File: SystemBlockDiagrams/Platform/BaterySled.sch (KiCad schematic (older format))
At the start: 7 parts

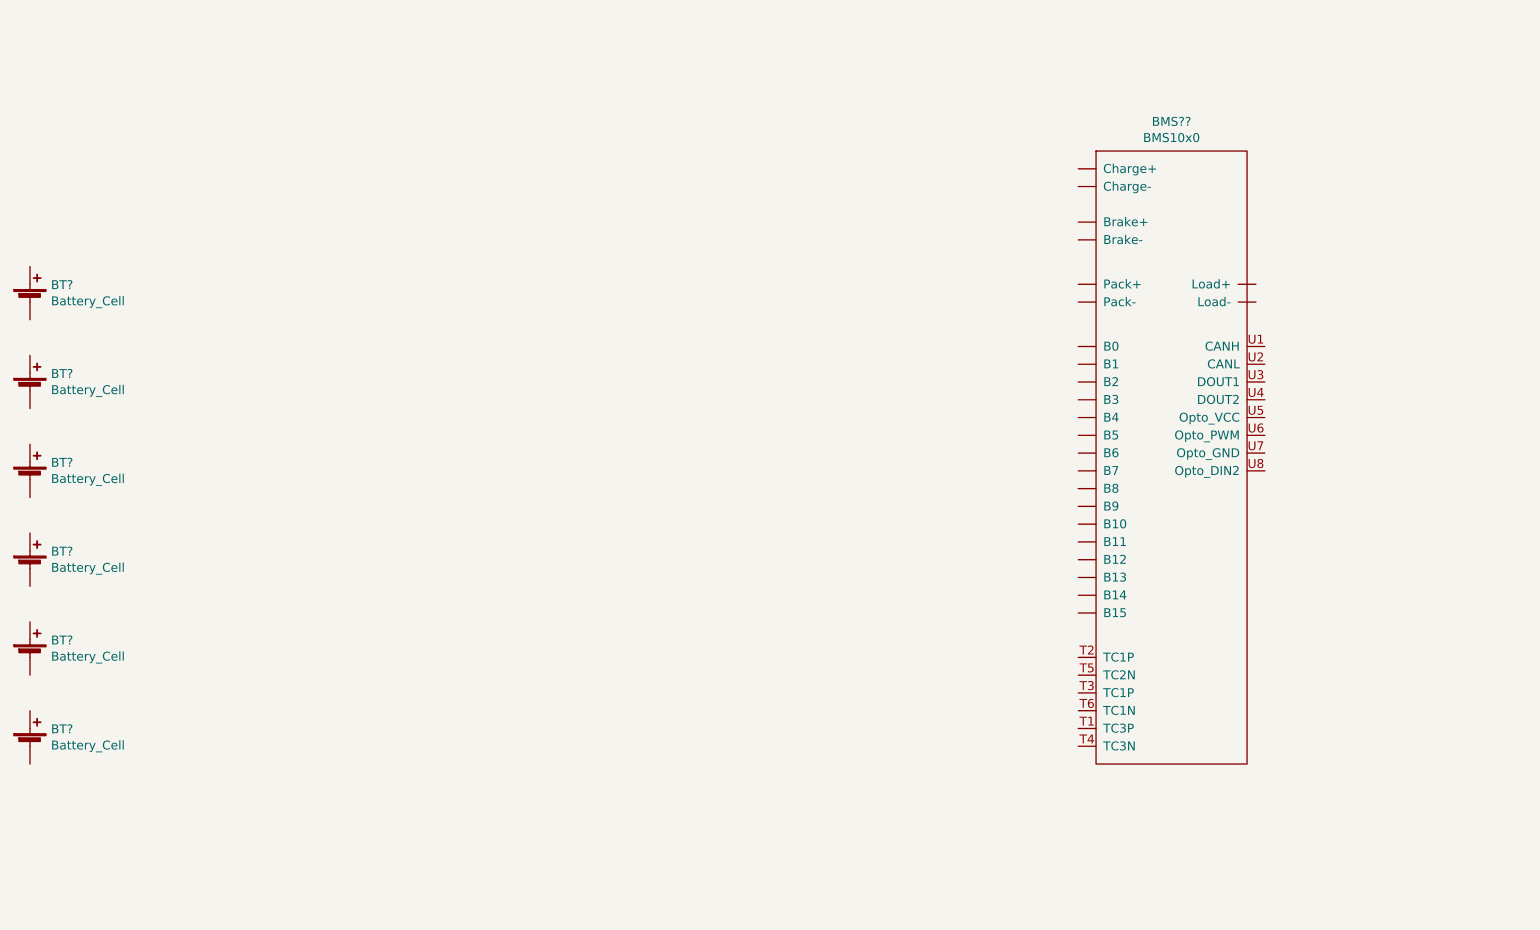
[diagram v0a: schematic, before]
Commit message: More platorm parts and connectors
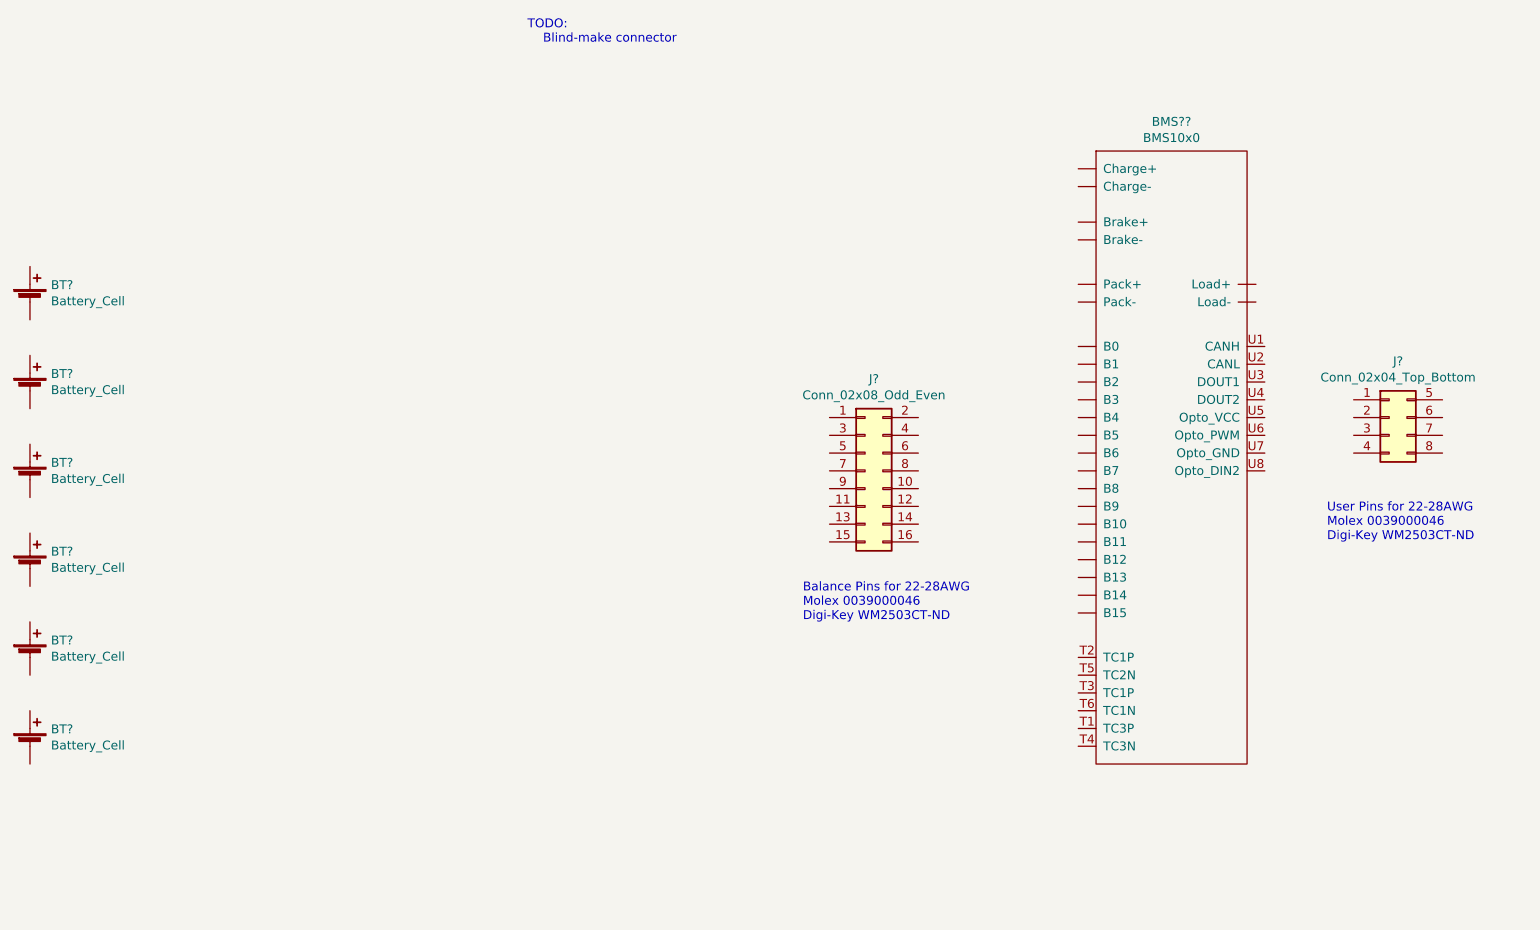
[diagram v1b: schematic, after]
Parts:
- added J?: Conn_02x08_Odd_Even, symbol Connector_Generic:Conn_02x08_Odd_Even
- added J?: Conn_02x04_Top_Bottom, symbol Connector_Generic:Conn_02x04_Top_Bottom
- BMS??: Supplier (none) -> Roboteq; Supplier Part Number (none) -> BMS1040
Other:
- note added: "Balance Pins for 22-28AWG\nMolex 0039000046\nDigi-Key WM2503CT-ND"
- note added: "TODO:\n Blind-make connector"
- note added: "User Pins for 22-28AWG\nMolex 0039000046\nDigi-Key WM2503CT-ND"
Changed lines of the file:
@@
 F 1 "BMS10x0" H 8175 3074 50  0000 C CNN
 F 2 "" H 7950 2350 50  0001 C CNN
-F 3 "" H 7950 2350 50  0001 C CNN
+F 3 "https://www.roboteq.com/index.php/docman/bms-documents-and-files/bms-documents/datasheet/349-bms10x0-datasheet/file" H 7950 2350 50  0001 C CNN
+F 4 "Roboteq" H 7950 2350 50  0001 C CNN "Supplier"
+F 5 "BMS1040" H 7950 2350 50  0001 C CNN "Supplier Part Number"
 	1    7950 2350
 	1    0    0    -1
@@
 	1    0    0    -1
 $EndComp
+Text Notes 4550 1100 0    50   ~ 0
+TODO:\n    Blind-make connector
+$Comp
+L Connector_Generic:Conn_02x08_Odd_Even J?
+U 1 1 5E27E551
+P 6450 3500
+F 0 "J?" H 6500 4017 50  0000 C CNN
+F 1 "Conn_02x08_Odd_Even" H 6500 3926 50  0000 C CNN
+F 2 "" H 6450 3500 50  0001 C CNN
+F 3 "https://www.molex.com/pdm_docs/sd/039012160_sd.pdf" H 6450 3500 50  0001 C CNN
+F 4 "Molex" H 6450 3500 50  0001 C CNN "Manufacturer"
+F 5 "0039012160" H 6450 3500 50  0001 C CNN "Manufacturer Part Number"
+F 6 "Digi-Key" H 6450 3500 50  0001 C CNN "Supplier"
+F 7 "WM3707-ND" H 6450 3500 50  0001 C CNN "Supplier Part Number"
+	1    6450 3500
+	1    0    0    -1
+$EndComp
+Text Notes 6100 4350 0    50   ~ 0
+Balance Pins for 22-28AWG\nMolex 0039000046\nDigi-Key WM2503CT-ND
+$Comp
+L Connector_Generic:Conn_02x04_Top_Bottom J?
+U 1 1 5E28024A
+P 9400 3200
+F 0 "J?" H 9450 3517 50  0000 C CNN
+F 1 "Conn_02x04_Top_Bottom" H 9450 3426 50  0000 C CNN
+F 2 "" H 9400 3200 50  0001 C CNN
+F 3 "https://www.molex.com/pdm_docs/sd/039012080_sd.pdf" H 9400 3200 50  0001 C CNN
+F 4 "Molex" H 9400 3200 50  0001 C CNN "Manufacturer"
+F 5 "0039012080" H 9400 3200 50  0001 C CNN "Manufacturer Part Number"
+F 6 "Digi-Key" H 9400 3200 50  0001 C CNN "Supplier"
+F 7 "WM3703-ND" H 9400 3200 50  0001 C CNN "Supplier Part Number"
+	1    9400 3200
+	1    0    0    -1
+$EndComp
+Text Notes 9050 3900 0    50   ~ 0
+User Pins for 22-28AWG\nMolex 0039000046\nDigi-Key WM2503CT-ND
 $EndSCHEMATC

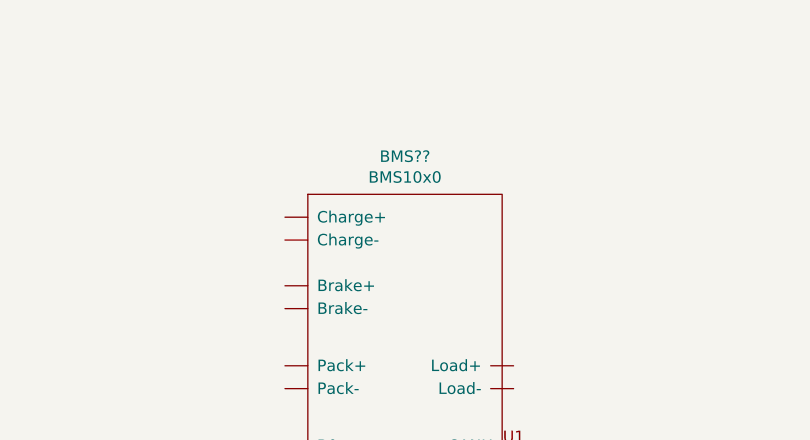
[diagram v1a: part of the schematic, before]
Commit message: Adjust electronics hierarchy to match mechanicals.
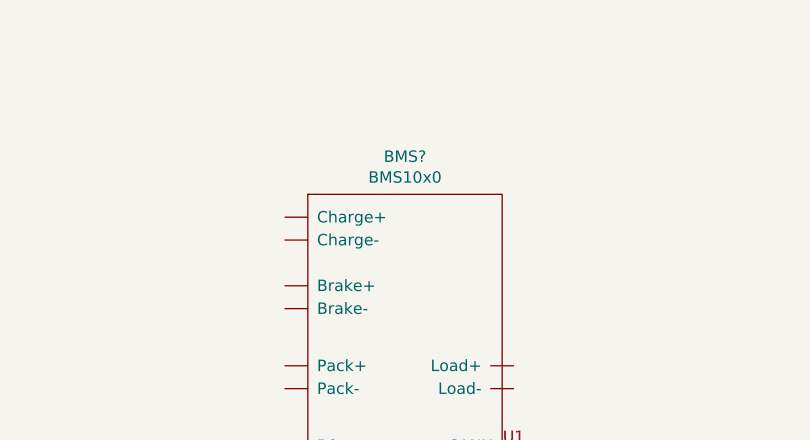
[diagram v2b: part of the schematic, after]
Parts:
- gave numbers to parts that had none: 1
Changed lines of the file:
@@
 $Descr A4 11693 8268
 encoding utf-8
-Sheet 15 15
+Sheet 15 16
 Title ""
 Date ""
@@
 $EndDescr
 $Comp
-L Stomp:BMS10x0 BMS??
+L Stomp:BMS10x0 BMS?
 U 1 1 5E270B30
 P 7950 2350
-F 0 "BMS??" H 8175 3165 50  0000 C CNN
+F 0 "BMS?" H 8175 3165 50  0000 C CNN
 F 1 "BMS10x0" H 8175 3074 50  0000 C CNN
 F 2 "" H 7950 2350 50  0001 C CNN

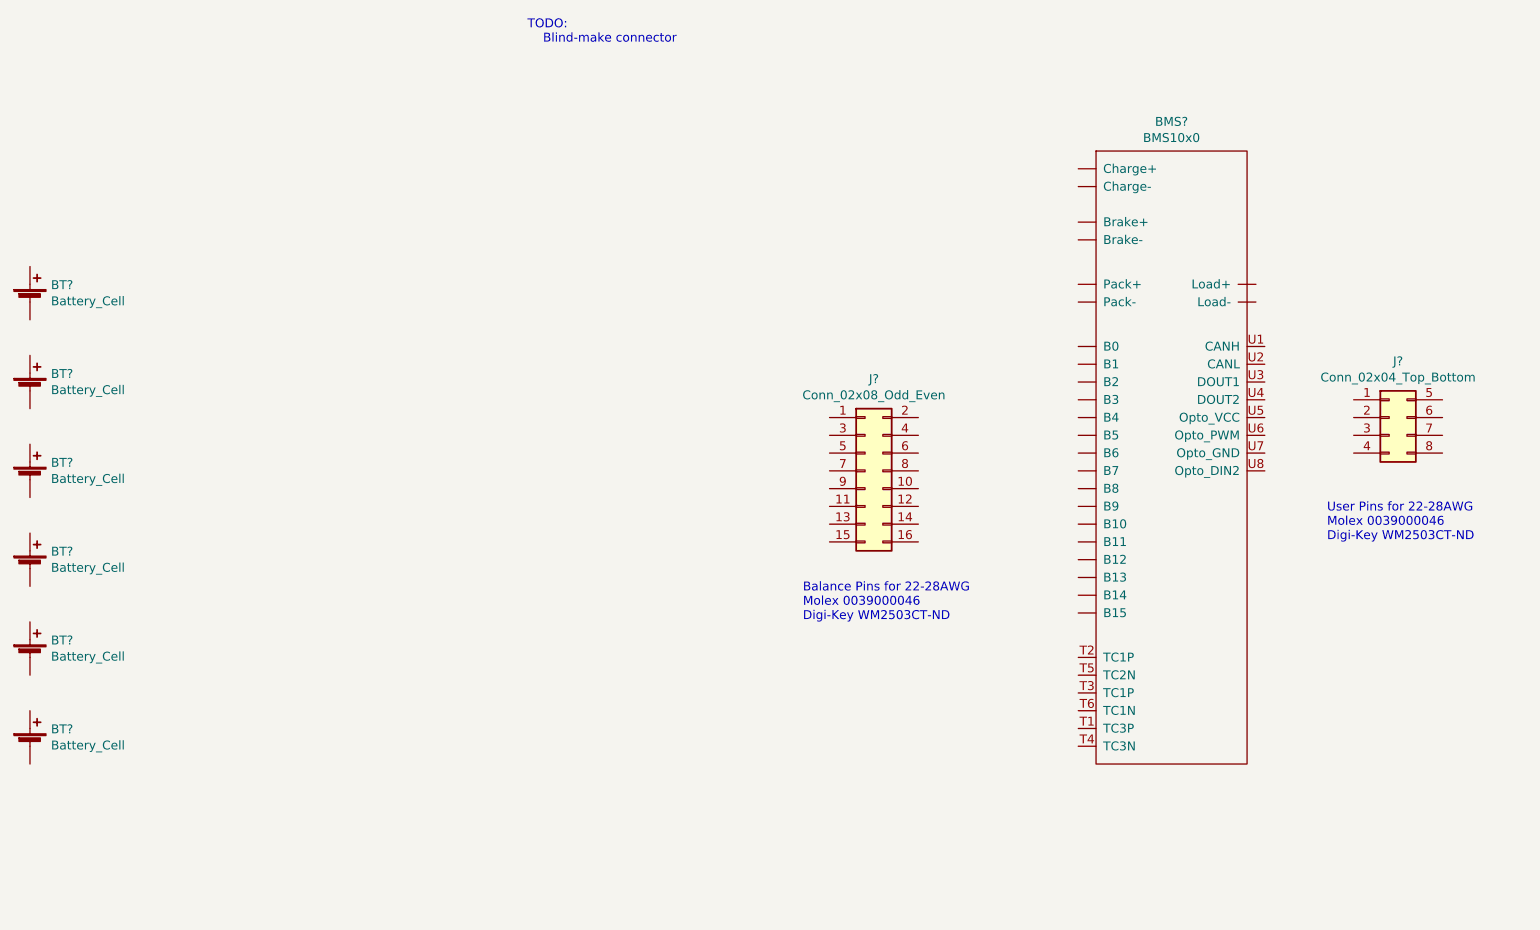
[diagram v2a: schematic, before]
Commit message: Update part numbers for BOM generation
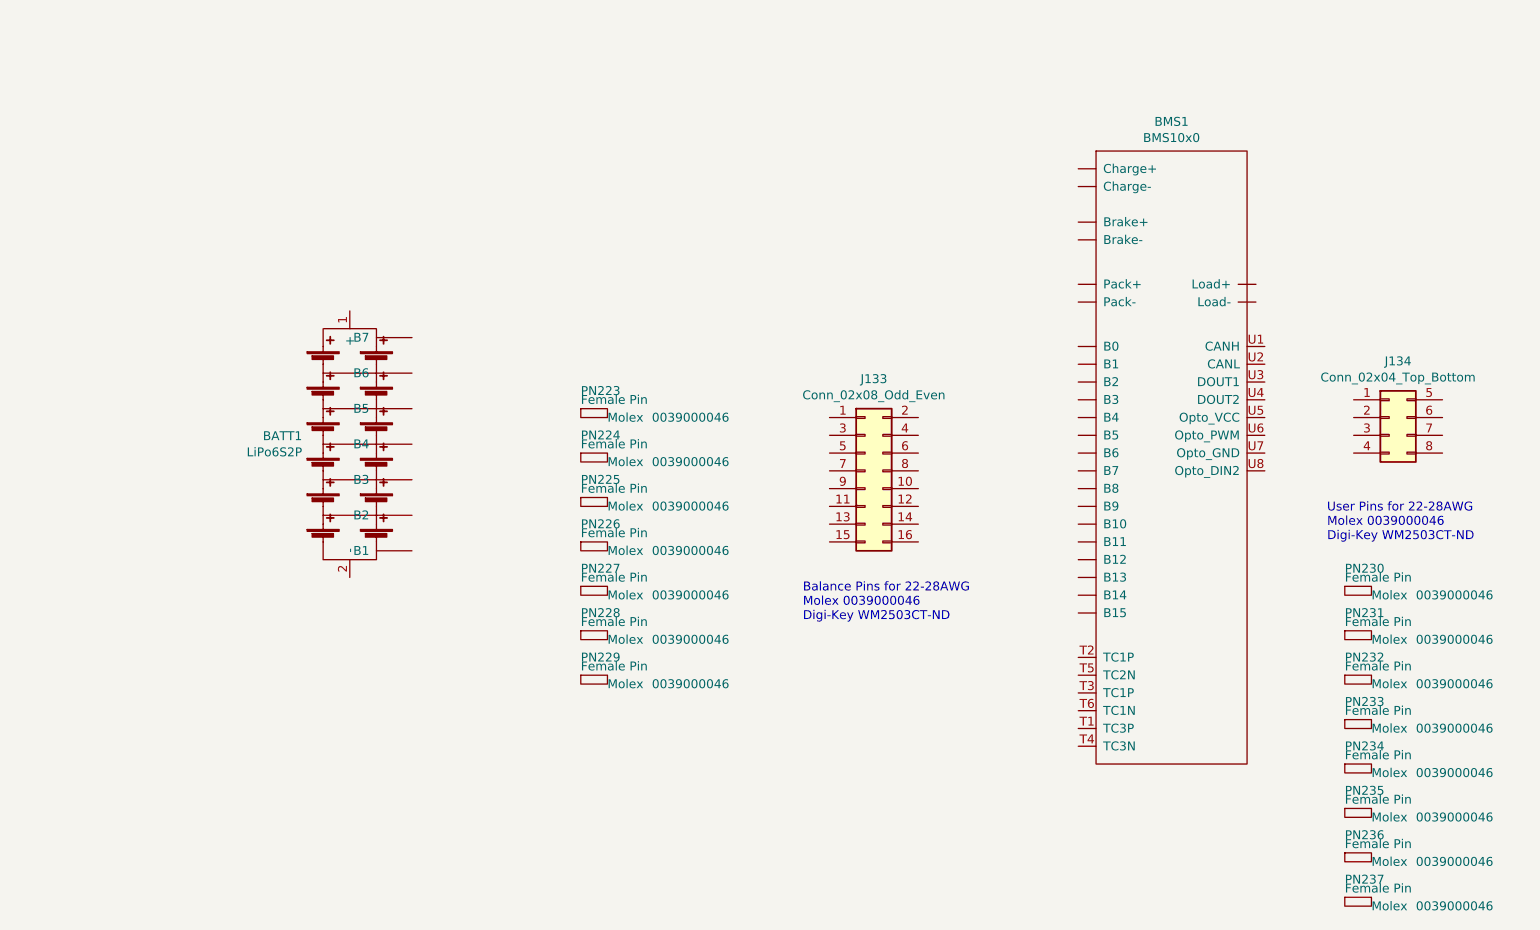
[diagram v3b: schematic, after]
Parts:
- removed BT? (x6): Battery_Cell, symbol Device:Battery_Cell
- added BATT1: LiPo6S2P, symbol Stomp:LiPo6S2P
- added PN223, PN224, PN225, PN226, PN227, PN228, PN229, PN230, PN231, PN232, PN233, PN234, PN235, PN236, PN237: Female Pin, symbol Stomp:PIN
- gave numbers to parts that had none: 3
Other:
- note removed: "TODO:\n Blind-make connector"
